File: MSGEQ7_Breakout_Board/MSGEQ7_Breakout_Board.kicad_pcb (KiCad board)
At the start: 2 copper layers, 44.4 x 25.4 mm, 10 parts, among them J1 BREAKOUT_BOARD_HEADER, J2 STEREO_MINI_JACK, U1 MSGEQ7

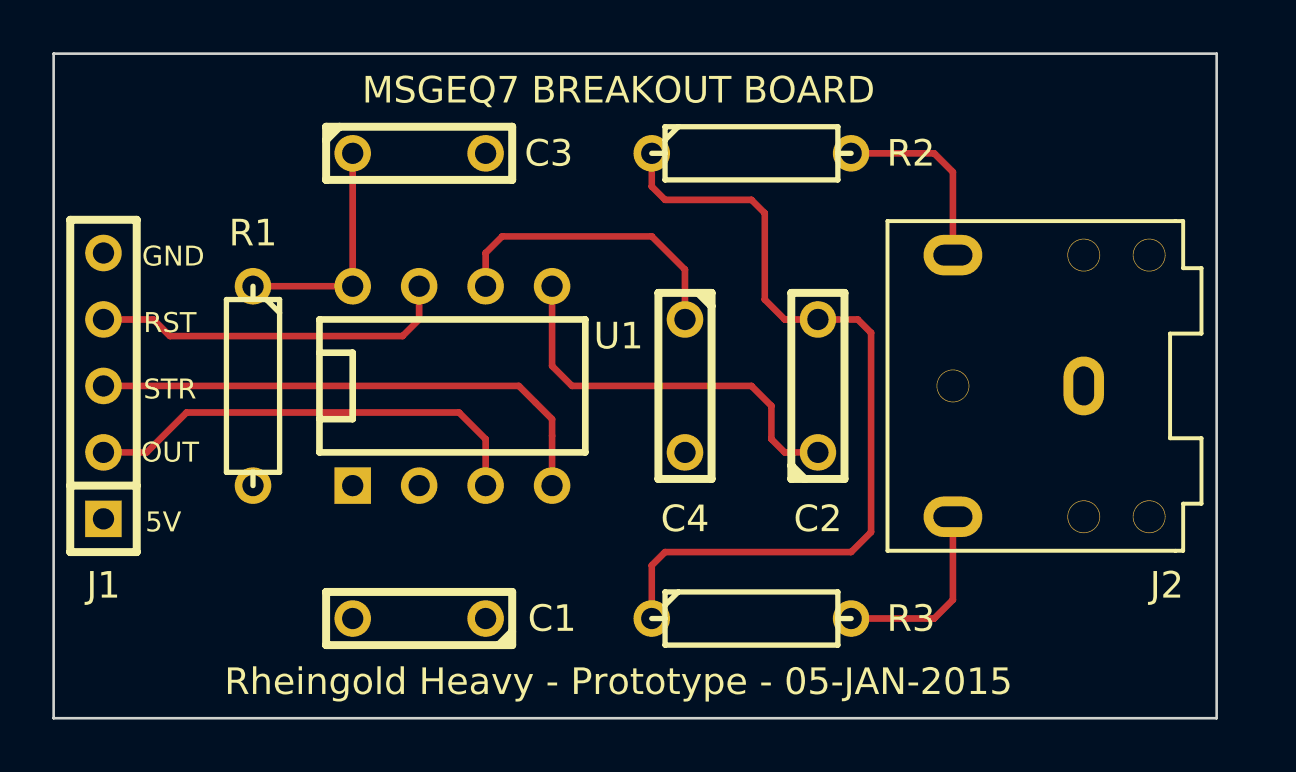
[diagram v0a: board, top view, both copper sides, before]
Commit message: First Gerbers Generated...
The gerbers check out fine in GERBV, however they are incompatible with
OSHParks service.  There are two drill files (PTH and Non-PTH) whereas
OSHPark expects only one.  Additionally, the oval drills for the 3.5mm
stereo jack pins is not registering as oval but circular which would not
allow the component to mount successfully. This will need to be
rectified with OSHPark Support tomorrow.
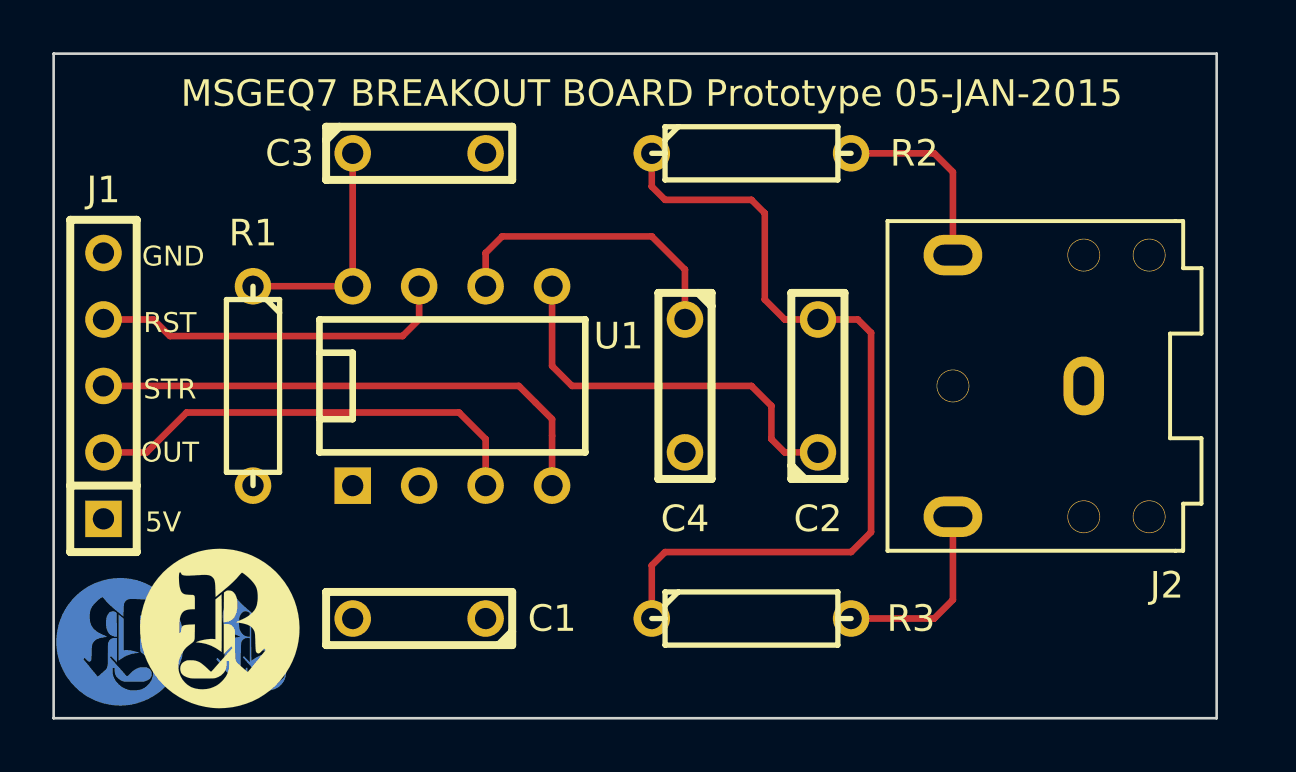
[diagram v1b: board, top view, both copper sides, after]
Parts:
- added VAL: REF, Logo_RH_Circle_R_B.SilkS_.2in_flipped, F.Cu at (233.2, 171.1)
- added VAL: REF, Logo_RH_Circle_R_B.SilkS_.1in_flipped, F.Cu at (227.3, 172.2)
- added VAL: REF, Logo_RH_Circle_R_B.Cu_.2in_flipped, F.Cu at (194.3, 172.3)
- added VAL: REF, Logo_RH_Circle_R_B.Mask_.2in_flipped, F.Cu at (194.3, 172.3)
- added VAL: REF, Logo_RH_Circle_R_B.SilkS_.2in_flipped, F.Cu at (199.4, 172.3)
- added VAL: REF, Logo_RH_Solo_R_B.Cu_.2in_flipped, F.Cu at (199.4, 172.3)
- added VAL: REF, Logo_RH_Solo_R_B.Mask_.2in_flipped, F.Cu at (199.4, 172.3)
- added VAL: REF, Logo_RH_Circle_R_F.SilkS_.25in, F.Cu at (198.1, 171.8)
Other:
- board text added: "100mil"
- board text added: "200mil"
- board text added: "MSGEQ7 BREAKOUT BOARD Prototype 05-JAN-2015"
- board text removed: "MSGEQ7 BREAKOUT BOARD"
- board text removed: "Rheingold Heavy - Prototype - 05-JAN-2015"

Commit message: Gerbers and Schematic Completed for Prototype
The layout was modified to accomodate non-oval drills and drill files
were merged.  All manufacturers, part numbers and datasheet fields have
been completed in the schematic.
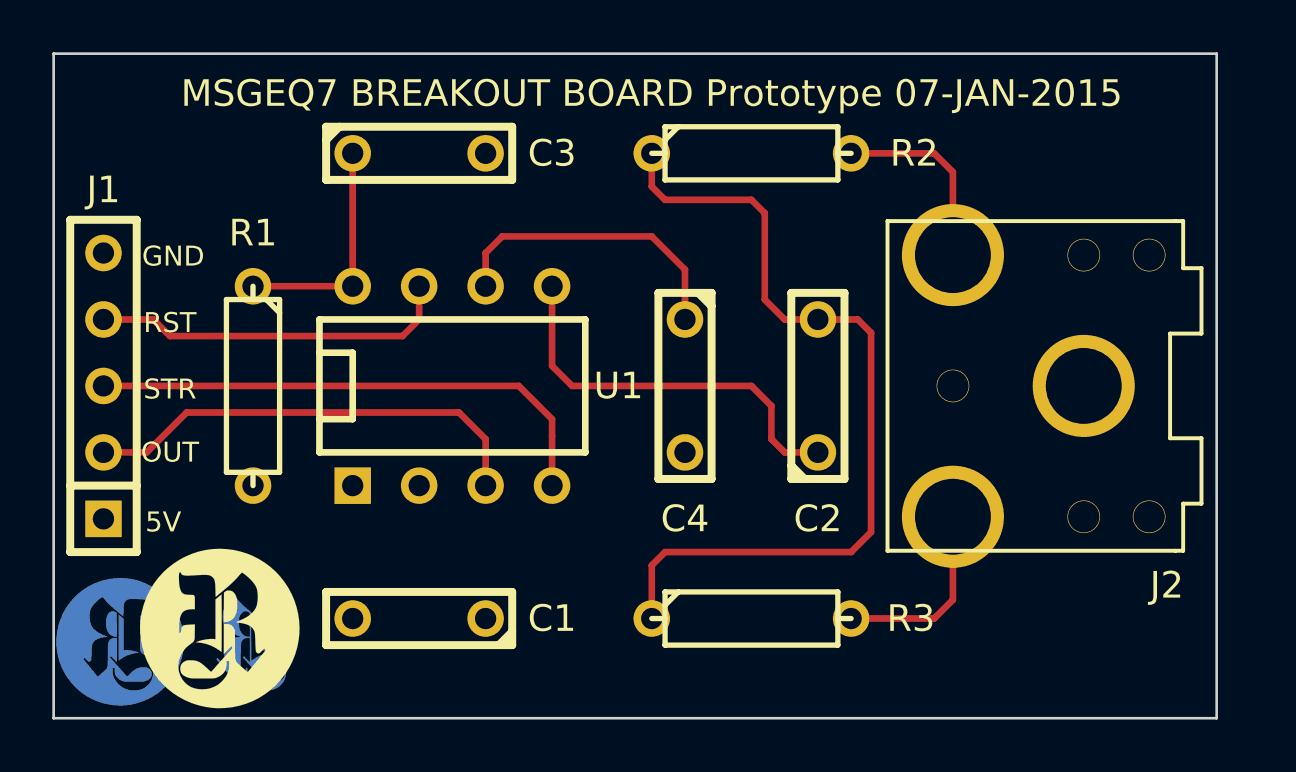
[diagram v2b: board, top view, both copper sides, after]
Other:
- board text added: "MSGEQ7 BREAKOUT BOARD Prototype 07-JAN-2015"
- board text removed: "MSGEQ7 BREAKOUT BOARD Prototype 05-JAN-2015"
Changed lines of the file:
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@@
   (page A3)
   (layers
-    (15 F.Cu signal hide)
+    (15 F.Cu signal)
     (0 B.Cu signal)
     (16 B.Adhes user)
@@
     (mod_text_size 1 1)
     (mod_text_width 0.15)
-    (pad_size 1.25 1.25)
-    (pad_drill 1.2)
+    (pad_size 3.9 3.9)
+    (pad_drill 2.9)
     (pad_to_mask_clearance 0)
     (aux_axis_origin 0 0)
@@
     (descr "8 pins DIL package, round pads")
     (tags DIL)
-    (fp_text reference U1 (at 6.35 -1.905) (layer F.SilkS)
+    (fp_text reference U1 (at 6.35 0) (layer F.SilkS)
       (effects (font (size 1.016 1.016) (thickness 0.2032)))
     )
@@
     (descr "Condensateur = 2 pas")
     (tags C)
-    (fp_text reference C3 (at -4.953 0) (layer F.SilkS)
+    (fp_text reference C3 (at 5.08 0) (layer F.SilkS)
       (effects (font (size 1.016 1.016) (thickness 0.254)))
     )
@@
       (scale (xyz 1 1 1))
       (rotate (xyz 0 0 0))
-    )
-  )
-  (module 3.5mm_Stereo_Jack_SJ1-3523NG (layer F.Cu)
-    (at 231.14 162.56 180)
-    (fp_text reference J2 (at -3.175 -7.62 180) (layer F.SilkS)
-      (effects (font (size 1.016 1.016) (thickness 0.254)))
-    )
-    (fp_text value STEREO_MINI_JACK (at 0 7.9 180) (layer F.SilkS) hide
-      (effects (font (size 1 1) (thickness 0.15)))
-    )
-    (fp_line (start -3.8 -4.5) (end -4.5 -4.5) (layer F.SilkS) (width 0.15))
-    (fp_line (start -3.5 -6.3) (end -3.8 -6.3) (layer F.SilkS) (width 0.15))
-    (fp_line (start -3.8 -4.5) (end -3.8 -6.3) (layer F.SilkS) (width 0.15))
-    (fp_line (start -3.8 4.5) (end -4.5 4.5) (layer F.SilkS) (width 0.15))
-    (fp_line (start -3.5 6.3) (end -3.8 6.3) (layer F.SilkS) (width 0.15))
-    (fp_line (start -3.8 6.3) (end -3.8 4.5) (layer F.SilkS) (width 0.15))
-    (fp_line (start 7.5 6.3) (end -3.5 6.3) (layer F.SilkS) (width 0.15))
-    (fp_line (start 7.5 -6.3) (end -3.5 -6.3) (layer F.SilkS) (width 0.15))
-    (fp_line (start 7.5 -6.3) (end 7.5 6.3) (layer F.SilkS) (width 0.15))
-    (fp_line (start -4.5 4.5) (end -4.5 2) (layer F.SilkS) (width 0.15))
-    (fp_line (start -4.5 -4.5) (end -4.5 -2) (layer F.SilkS) (width 0.15))
-    (fp_line (start -4.5 -2) (end -3.3 -2) (layer F.SilkS) (width 0.15))
-    (fp_line (start -3.3 -2) (end -3.3 2) (layer F.SilkS) (width 0.15))
-    (fp_line (start -3.3 2) (end -4.5 2) (layer F.SilkS) (width 0.15))
-    (pad 1 thru_hole oval (at 0 0 180) (size 1.55 2.25) (drill oval 0.8 1.5)
-      (layers *.Cu *.Mask F.SilkS)
-      (net 2 GND)
-    )
-    (pad 2 thru_hole oval (at 5 5 180) (size 2.25 1.55) (drill oval 1.5 0.8)
-      (layers *.Cu *.Mask F.SilkS)
-      (net 5 N-000002)
-    )
-    (pad 3 thru_hole oval (at 5 -5 180) (size 2.25 1.55) (drill oval 1.5 0.8)
-      (layers *.Cu *.Mask F.SilkS)
-      (net 8 N-000006)
-    )
-    (pad "" np_thru_hole circle (at 5 0 180) (size 1.25 1.25) (drill 1.2)
-      (layers *.Cu *.Mask F.SilkS)
-    )
-    (pad "" np_thru_hole circle (at 0 -5 180) (size 1.25 1.25) (drill 1.2)
-      (layers *.Cu *.Mask F.SilkS)
-    )
-    (pad "" np_thru_hole circle (at 0 5 180) (size 1.25 1.25) (drill 1.2)
-      (layers *.Cu *.Mask F.SilkS)
-    )
-    (pad "" np_thru_hole circle (at -2.5 5 180) (size 1.25 1.25) (drill 1.2)
-      (layers *.Cu *.Mask F.SilkS)
-    )
-    (pad "" np_thru_hole circle (at -2.5 -5 180) (size 1.25 1.25) (drill 1.2)
-      (layers *.Cu *.Mask F.SilkS)
     )
   )
@@
       (xy 0.6731 -0.91186)) (layer F.SilkS) (width 0.00254))
   )
+  (module 3.5mm_Stereo_Jack_SJ1-3523NG (layer F.Cu)
+    (at 231.14 162.56 180)
+    (fp_text reference J2 (at -3.175 -7.62 180) (layer F.SilkS)
+      (effects (font (size 1.016 1.016) (thickness 0.254)))
+    )
+    (fp_text value STEREO_MINI_JACK (at 0 7.9 180) (layer F.SilkS) hide
+      (effects (font (size 1 1) (thickness 0.15)))
+    )
+    (fp_line (start -3.8 -4.5) (end -4.5 -4.5) (layer F.SilkS) (width 0.15))
+    (fp_line (start -3.5 -6.3) (end -3.8 -6.3) (layer F.SilkS) (width 0.15))
+    (fp_line (start -3.8 -4.5) (end -3.8 -6.3) (layer F.SilkS) (width 0.15))
+    (fp_line (start -3.8 4.5) (end -4.5 4.5) (layer F.SilkS) (width 0.15))
+    (fp_line (start -3.5 6.3) (end -3.8 6.3) (layer F.SilkS) (width 0.15))
+    (fp_line (start -3.8 6.3) (end -3.8 4.5) (layer F.SilkS) (width 0.15))
+    (fp_line (start 7.5 6.3) (end -3.5 6.3) (layer F.SilkS) (width 0.15))
+    (fp_line (start 7.5 -6.3) (end -3.5 -6.3) (layer F.SilkS) (width 0.15))
+    (fp_line (start 7.5 -6.3) (end 7.5 6.3) (layer F.SilkS) (width 0.15))
+    (fp_line (start -4.5 4.5) (end -4.5 2) (layer F.SilkS) (width 0.15))
+    (fp_line (start -4.5 -4.5) (end -4.5 -2) (layer F.SilkS) (width 0.15))
+    (fp_line (start -4.5 -2) (end -3.3 -2) (layer F.SilkS) (width 0.15))
+    (fp_line (start -3.3 -2) (end -3.3 2) (layer F.SilkS) (width 0.15))
+    (fp_line (start -3.3 2) (end -4.5 2) (layer F.SilkS) (width 0.15))
+    (pad 1 thru_hole circle (at 0 0 180) (size 3.9 3.9) (drill 2.9)
+      (layers *.Cu *.Mask F.SilkS)
+      (net 2 GND)
+    )
+    (pad 2 thru_hole circle (at 5 5 180) (size 3.9 3.9) (drill 2.9)
+      (layers *.Cu *.Mask F.SilkS)
+      (net 5 N-000002)
+    )
+    (pad 3 thru_hole circle (at 5 -5 180) (size 3.9 3.9) (drill 2.9)
+      (layers *.Cu *.Mask F.SilkS)
+      (net 8 N-000006)
+    )
+    (pad "" np_thru_hole circle (at 5 0 180) (size 1.25 1.25) (drill 1.2)
+      (layers *.Cu *.Mask F.SilkS)
+    )
+    (pad "" np_thru_hole circle (at 0 -5 180) (size 1.25 1.25) (drill 1.2)
+      (layers *.Cu *.Mask F.SilkS)
+    )
+    (pad "" np_thru_hole circle (at 0 5 180) (size 1.25 1.25) (drill 1.2)
+      (layers *.Cu *.Mask F.SilkS)
+    )
+    (pad "" np_thru_hole circle (at -2.5 5 180) (size 1.25 1.25) (drill 1.2)
+      (layers *.Cu *.Mask F.SilkS)
+    )
+    (pad "" np_thru_hole circle (at -2.5 -5 180) (size 1.25 1.25) (drill 1.2)
+      (layers *.Cu *.Mask F.SilkS)
+    )
+  )
   (gr_text 100mil (at 227.076 174.498) (layer B.SilkS)
     (effects (font (size 1.016 1.016) (thickness 0.254)) (justify mirror))
@@
     (effects (font (size 1.016 1.016) (thickness 0.254)) (justify mirror))
   )
-  (gr_text "MSGEQ7 BREAKOUT BOARD Prototype 05-JAN-2015" (at 214.63 151.384) (layer F.SilkS)
+  (gr_text "MSGEQ7 BREAKOUT BOARD Prototype 07-JAN-2015" (at 214.63 151.384) (layer F.SilkS)
     (effects (font (size 1.016 1.016) (thickness 0.254)))
   )
